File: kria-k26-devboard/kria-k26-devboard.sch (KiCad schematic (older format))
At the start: 2 parts

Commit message: Added second ETH interface, connect POE PSE
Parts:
- removed N?: antmicro_logo, antmicro-footprints:antmicro-logo, symbol antmicroMechanicalParts:antmicro_logo
- gave numbers to parts that had none: 1
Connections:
- wire segments 283 -> 289
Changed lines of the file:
@@
 F1 "eth.sch" 50
 F2 "MIO[64..77]" I L 9850 1200 50
-F3 "POE_VC[1..4]" I L 9850 900 50
+F3 "POE_VC[1..4]" I L 9850 850 50
 F4 "ETH_RESET" I R 11550 900 50
-$EndSheet
-$Sheet
-S 4350 800  1600 900
+F5 "VDD_POE_OUT" I L 9850 950 50
+F6 "VSS_POE_OUT" I L 9850 1050 50
+$EndSheet
+$Sheet
+S 4350 650  1600 1100
 U 63C44BC2
 F0 "Power Supply" 50
 F1 "supply.sch" 50
 F2 "PD_CC[1..2]" I R 5950 1550 50
-F3 "VCCOEN_PS_M2C" I R 5950 1000 50
-F4 "VCCOEN_PL_M2C" I R 5950 1100 50
-F5 "POE_VC[1..4]" I R 5950 900 50
-F6 "DBG_USB_P" I R 5950 1250 50
-F7 "DBG_USB_N" I R 5950 1400 50
+F3 "VCCOEN_PS_M2C" I R 5950 1100 50
+F4 "VCCOEN_PL_M2C" I R 5950 1200 50
+F5 "POE_VC[1..4]" I R 5950 700 50
+F6 "DBG_USB_P" I R 5950 1300 50
+F7 "DBG_USB_N" I R 5950 1450 50
 F8 "VBUS" I R 5950 1650 50
+F9 "VDD_POE_OUT" I R 5950 850 50
+F10 "VSS_POE_OUT" I R 5950 950 50
 $EndSheet
 $Sheet
@@
 F13 "~PS_POR" I L 4350 3150 50
 $EndSheet
-Wire Bus Line
-	5950 900  9850 900
-Wire Wire Line
-	5950 1100 6400 1100
+Wire Wire Line
+	5950 1200 6400 1200
 $Sheet
 S 9850 5250 1700 1300
@@
 	6000 2250 6000 2300
 Wire Wire Line
-	6250 1350 6000 1350
-Wire Wire Line
-	6000 1350 6000 1400
-Wire Wire Line
-	6000 1400 5950 1400
-Wire Wire Line
 	6000 2300 6250 2300
 Wire Wire Line
-	5950 1000 6500 1000
-Wire Wire Line
 	6500 1200 7050 1200
 Wire Wire Line
 	6400 1300 7050 1300
-Wire Wire Line
-	5950 1250 6000 1250
-Wire Wire Line
-	6000 1250 6000 1300
-Wire Wire Line
-	6000 1300 6300 1300
 Wire Wire Line
 	6300 2350 6000 2350
@@
 Wire Wire Line
 	7000 6300 6000 6300
-Wire Wire Line
-	6500 1000 6500 1200
-Wire Wire Line
-	6400 1100 6400 1300
 Wire Bus Line
 	6150 1550 5950 1550
 Wire Wire Line
-	6250 1350 6250 2300
-Wire Wire Line
-	6300 1300 6300 2350
-Wire Wire Line
 	5950 2000 6050 2000
 Wire Wire Line
 	6050 2000 6050 1650
-Wire Wire Line
-	6050 1650 5950 1650
 Wire Bus Line
 	5950 2100 6150 2100
@@
 	11650 8400 11650 10150
 $Comp
-L antmicroMechanicalParts:oshw_logo N?
+L antmicroMechanicalParts:oshw_logo N2
 U 1 1 63FCC534
 P 700 11000
-F 0 "N?" H 894 11003 50  0000 L CNN
+F 0 "N2" H 894 11003 50  0000 L CNN
 F 1 "oshw_logo" H 894 10912 50  0000 L CNN
 F 2 "antmicro-footprints:oshw-logo" H 720 10760 50  0001 C CNN
@@
 	1    0    0    -1
 $EndComp
-$Comp
-L antmicroMechanicalParts:antmicro_logo N?
-U 1 1 63FCC88F
-P 650 10850
-F 0 "N?" H 864 10943 50  0000 L CNN
-F 1 "antmicro_logo" H 864 10852 50  0000 L CNN
-F 2 "antmicro-footprints:antmicro-logo" H 550 11100 50  0001 C CNN
-F 3 "" H 650 11200 50  0001 C CNN
-	1    650  10850
-	1    0    0    -1
-$EndComp
 $Sheet
 S 9850 8700 1700 650
@@
 Wire Wire Line
 	6350 8250 7050 8250
+Wire Wire Line
+	6000 1300 6000 1350
+Wire Wire Line
+	5950 1300 6000 1300
+Wire Wire Line
+	6000 1450 5950 1450
+Wire Wire Line
+	6000 1400 6000 1450
+Wire Wire Line
+	6250 1400 6000 1400
+Wire Wire Line
+	6250 1400 6250 2300
+Wire Wire Line
+	6300 1350 6300 2350
+Wire Wire Line
+	6000 1350 6300 1350
+Wire Wire Line
+	6400 1200 6400 1300
+Wire Wire Line
+	6500 1100 6500 1200
+Wire Wire Line
+	5950 1100 6500 1100
+Wire Wire Line
+	6050 1650 5950 1650
+Wire Bus Line
+	5950 700  9700 700
+Wire Bus Line
+	9700 700  9700 850
+Wire Bus Line
+	9700 850  9850 850
+Wire Wire Line
+	9850 950  9600 950
+Wire Wire Line
+	9600 950  9600 850
+Wire Wire Line
+	9600 850  5950 850
+Wire Wire Line
+	9850 1050 9500 1050
+Wire Wire Line
+	9500 1050 9500 950
+Wire Wire Line
+	9500 950  5950 950
 $EndSCHEMATC

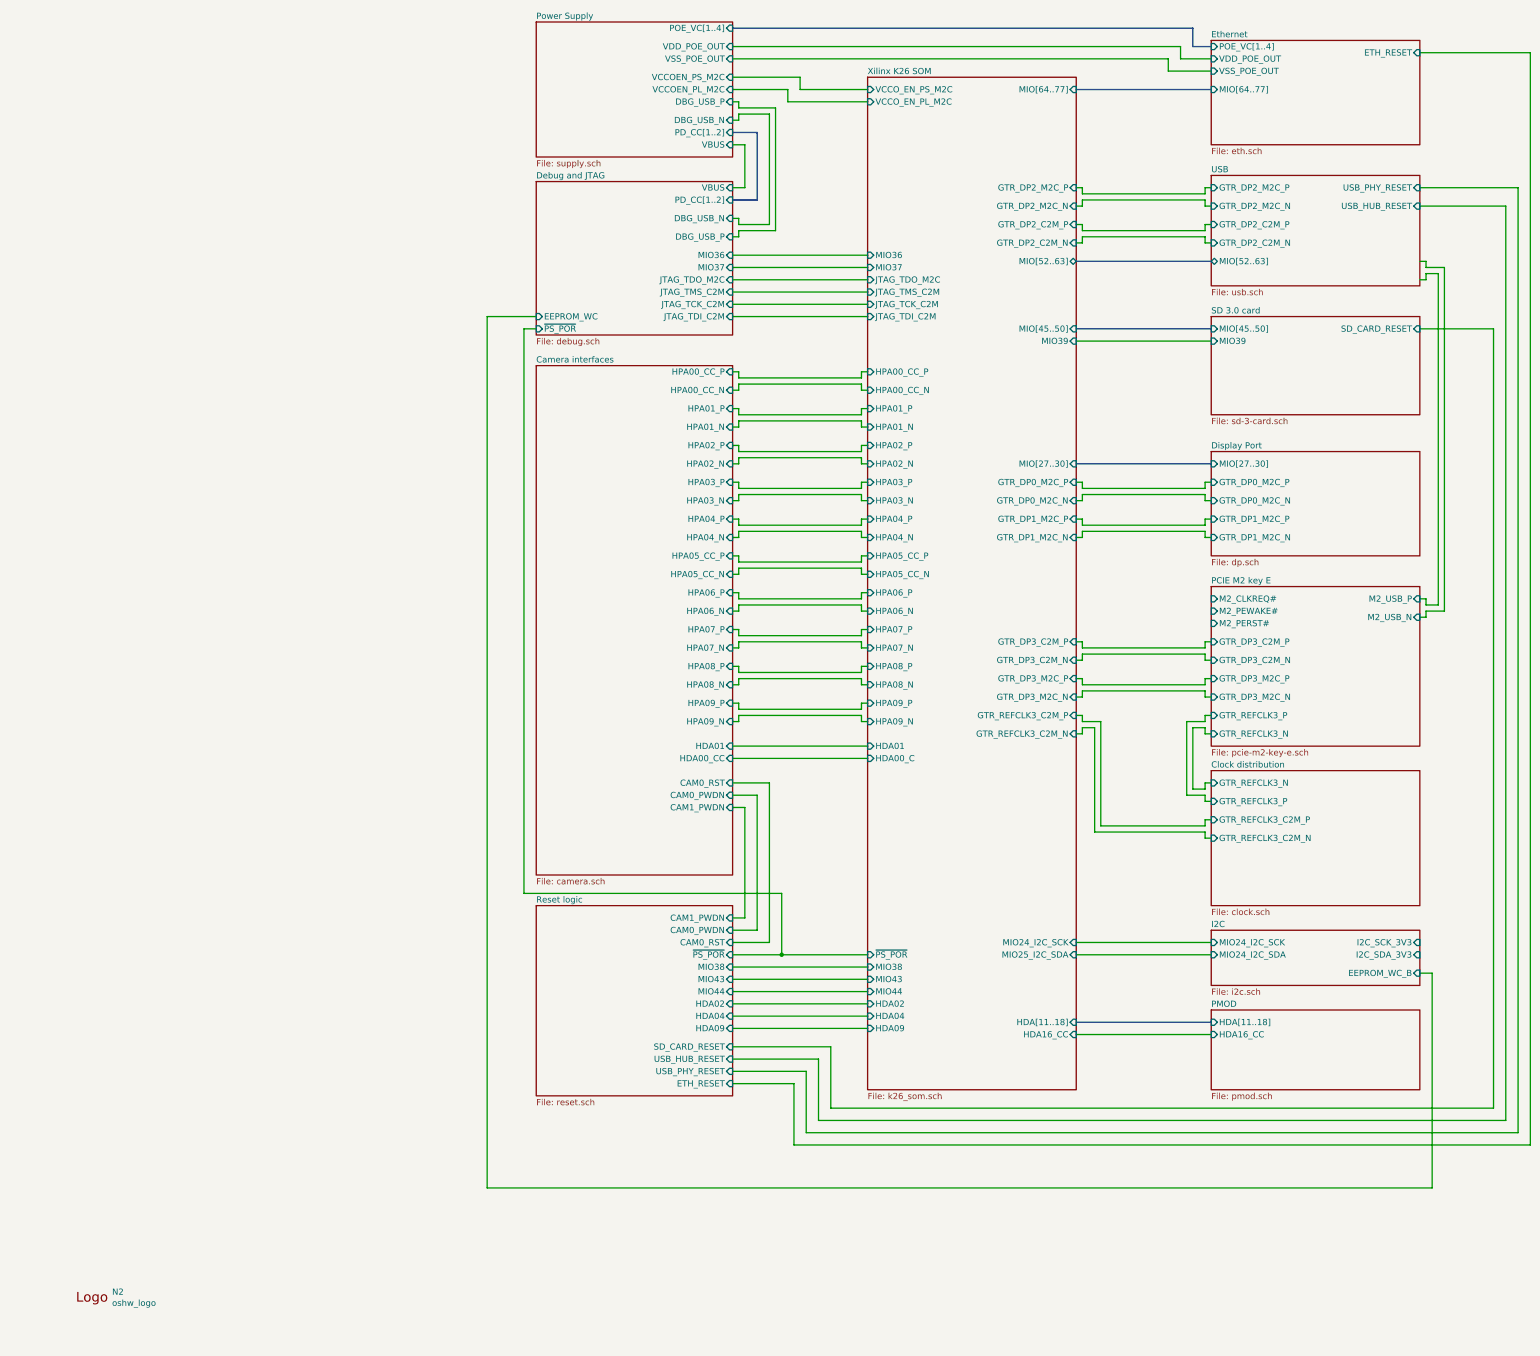
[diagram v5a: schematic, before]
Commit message: Fixes on Reset pagae, progress through clock sheet
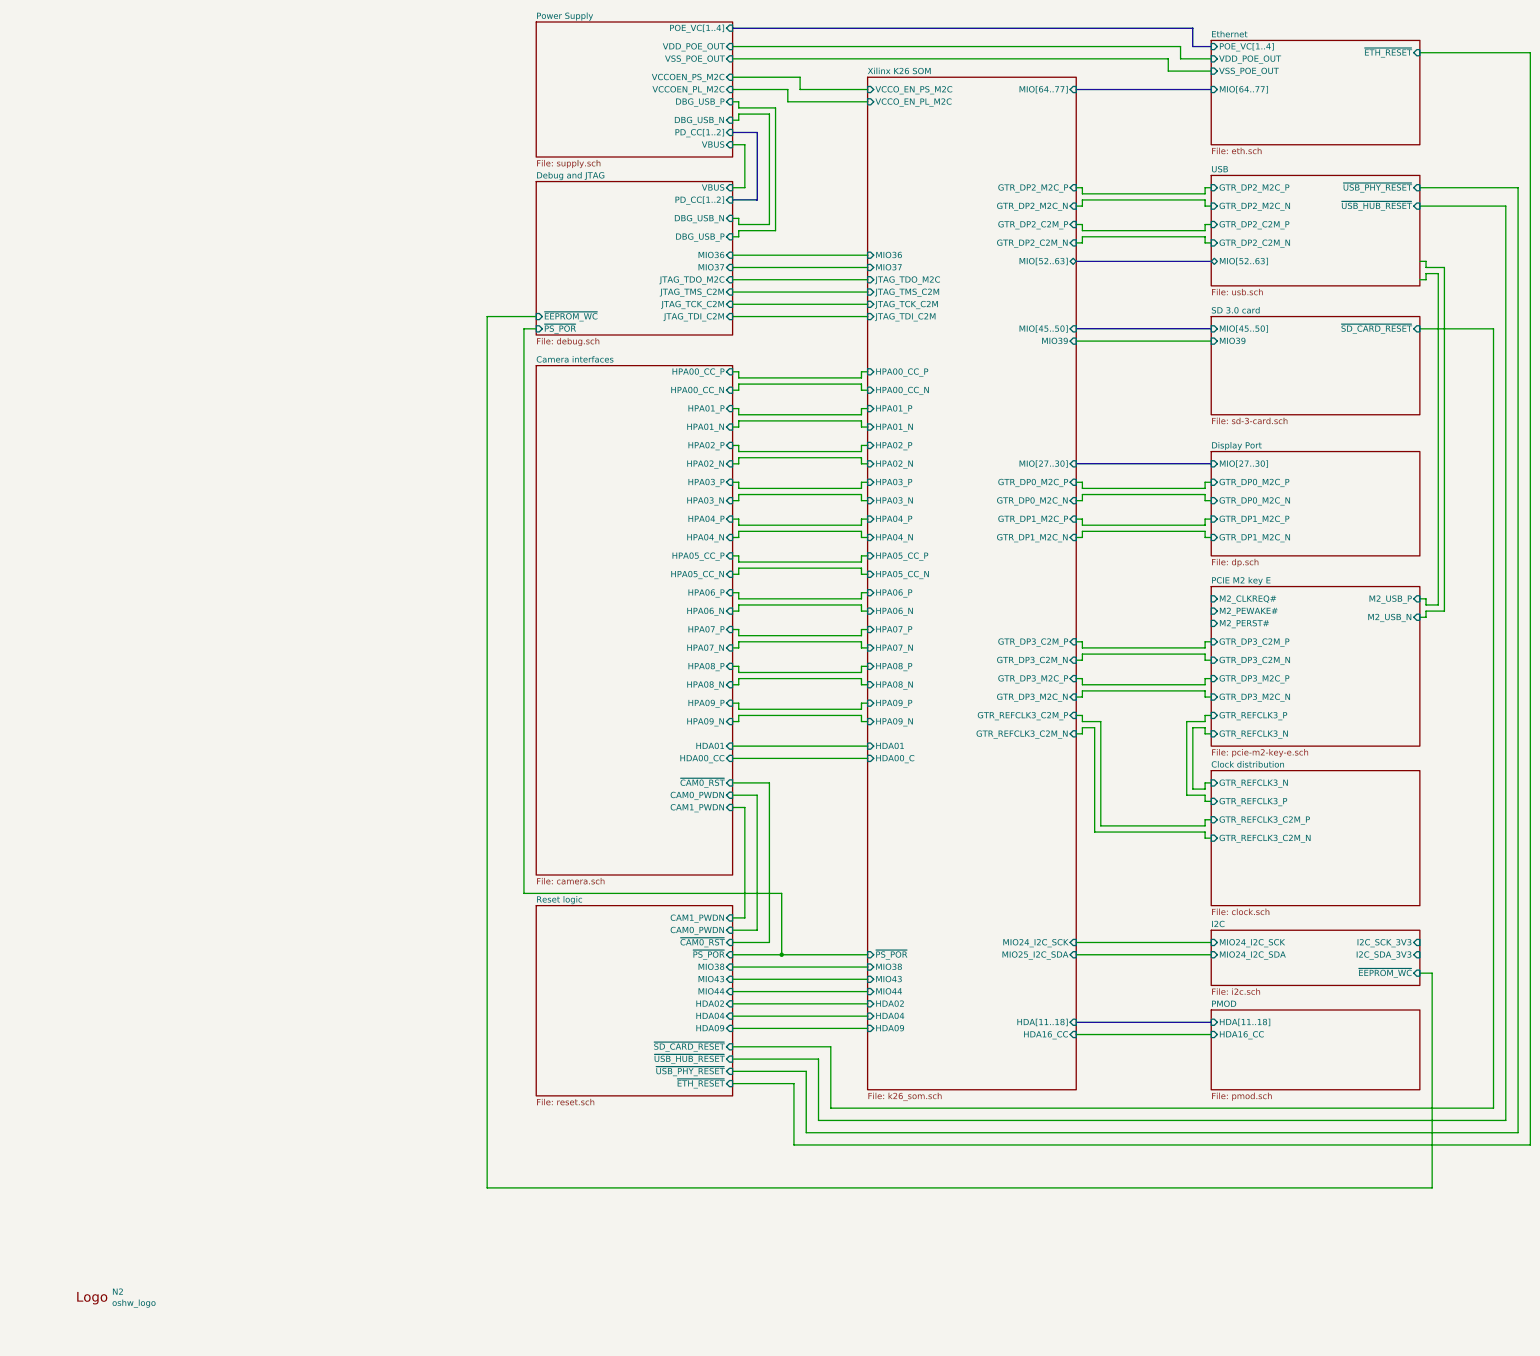
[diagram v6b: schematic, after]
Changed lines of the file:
@@
 $EndDescr
-$Sheet
-S 9850 800  1700 850
-U 63C3FA95
-F0 "Ethernet" 50
-F1 "eth.sch" 50
-F2 "MIO[64..77]" I L 9850 1200 50
-F3 "POE_VC[1..4]" I L 9850 850 50
-F4 "ETH_RESET" I R 11550 900 50
-F5 "VDD_POE_OUT" I L 9850 950 50
-F6 "VSS_POE_OUT" I L 9850 1050 50
-$EndSheet
 $Sheet
 S 4350 650  1600 1100
@@
 F9 "VDD_POE_OUT" I R 5950 850 50
 F10 "VSS_POE_OUT" I R 5950 950 50
-$EndSheet
-$Sheet
-S 9850 1900 1700 900
-U 63CADD16
-F0 "USB" 50
-F1 "usb.sch" 50
-F2 "MIO[52..63]" B L 9850 2600 50
-F3 "GTR_DP2_C2M_P" I L 9850 2300 50
-F4 "GTR_DP2_C2M_N" I L 9850 2450 50
-F5 "GTR_DP2_M2C_P" I L 9850 2000 50
-F6 "GTR_DP2_M2C_N" I L 9850 2150 50
-F7 "USB_PHY_RESET" I R 11550 2000 50
-F8 "USB_HUB_RESET" I R 11550 2150 50
 $EndSheet
 $Sheet
@@
 F10 "MIO36" I R 5950 2550 50
 F11 "VBUS" I R 5950 2000 50
-F12 "EEPROM_WC" I L 4350 3050 50
-F13 "~PS_POR" I L 4350 3150 50
+F12 "~PS_POR" I L 4350 3150 50
+F13 "~EEPROM_WC" I L 4350 3050 50
 $EndSheet
 Wire Wire Line
@@
 F2 "MIO[45..50]" I L 9850 3150 50
 F3 "MIO39" I L 9850 3250 50
-F4 "SD_CARD_RESET" I R 11550 3150 50
+F4 "~SD_CARD_RESET" I R 11550 3150 50
 $EndSheet
 Wire Wire Line
@@
 F22 "HDA01" I R 5950 6550 50
 F23 "HDA00_CC" I R 5950 6650 50
-F24 "CAM0_RST" I R 5950 6850 50
-F25 "CAM0_PWDN" I R 5950 6950 50
-F26 "CAM1_PWDN" I R 5950 7050 50
+F24 "CAM0_PWDN" I R 5950 6950 50
+F25 "CAM1_PWDN" I R 5950 7050 50
+F26 "~CAM0_RST" I R 5950 6850 50
 $EndSheet
 Wire Wire Line
@@
 F0 "Reset logic" 50
 F1 "reset.sch" 50
-F2 "SD_CARD_RESET" I R 5950 9000 50
-F3 "USB_PHY_RESET" I R 5950 9200 50
-F4 "USB_HUB_RESET" I R 5950 9100 50
-F5 "ETH_RESET" I R 5950 9300 50
-F6 "MIO43" I R 5950 8450 50
-F7 "MIO44" I R 5950 8550 50
-F8 "MIO38" I R 5950 8350 50
-F9 "CAM0_RST" I R 5950 8150 50
-F10 "CAM0_PWDN" I R 5950 8050 50
-F11 "CAM1_PWDN" I R 5950 7950 50
-F12 "HDA02" I R 5950 8650 50
-F13 "HDA04" I R 5950 8750 50
-F14 "HDA09" I R 5950 8850 50
-F15 "~PS_POR" I R 5950 8250 50
+F2 "MIO43" I R 5950 8450 50
+F3 "MIO44" I R 5950 8550 50
+F4 "MIO38" I R 5950 8350 50
+F5 "CAM0_PWDN" I R 5950 8050 50
+F6 "CAM1_PWDN" I R 5950 7950 50
+F7 "HDA02" I R 5950 8650 50
+F8 "HDA04" I R 5950 8750 50
+F9 "HDA09" I R 5950 8850 50
+F10 "~PS_POR" I R 5950 8250 50
+F11 "~USB_PHY_RESET" I R 5950 9200 50
+F12 "~USB_HUB_RESET" I R 5950 9100 50
+F13 "~ETH_RESET" I R 5950 9300 50
+F14 "~CAM0_RST" I R 5950 8150 50
+F15 "~SD_CARD_RESET" I R 5950 9000 50
 $EndSheet
 Wire Wire Line
@@
 F4 "I2C_SDA_3V3" I R 11550 8250 50
 F5 "I2C_SCK_3V3" I R 11550 8150 50
-F6 "EEPROM_WC_B" I R 11550 8400 50
+F6 "~EEPROM_WC" I R 11550 8400 50
 $EndSheet
 Wire Wire Line
@@
 Wire Wire Line
 	9500 950  5950 950
+$Sheet
+S 9850 1900 1700 900
+U 63CADD16
+F0 "USB" 50
+F1 "usb.sch" 50
+F2 "MIO[52..63]" B L 9850 2600 50
+F3 "GTR_DP2_C2M_P" I L 9850 2300 50
+F4 "GTR_DP2_C2M_N" I L 9850 2450 50
+F5 "GTR_DP2_M2C_P" I L 9850 2000 50
+F6 "GTR_DP2_M2C_N" I L 9850 2150 50
+F7 "~USB_PHY_RESET" I R 11550 2000 50
+F8 "~USB_HUB_RESET" I R 11550 2150 50
+$EndSheet
+$Sheet
+S 9850 800  1700 850
+U 63C3FA95
+F0 "Ethernet" 50
+F1 "eth.sch" 50
+F2 "MIO[64..77]" I L 9850 1200 50
+F3 "POE_VC[1..4]" I L 9850 850 50
+F4 "VDD_POE_OUT" I L 9850 950 50
+F5 "VSS_POE_OUT" I L 9850 1050 50
+F6 "~ETH_RESET" I R 11550 900 50
+$EndSheet
 $EndSCHEMATC

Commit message: Finished clock sheet
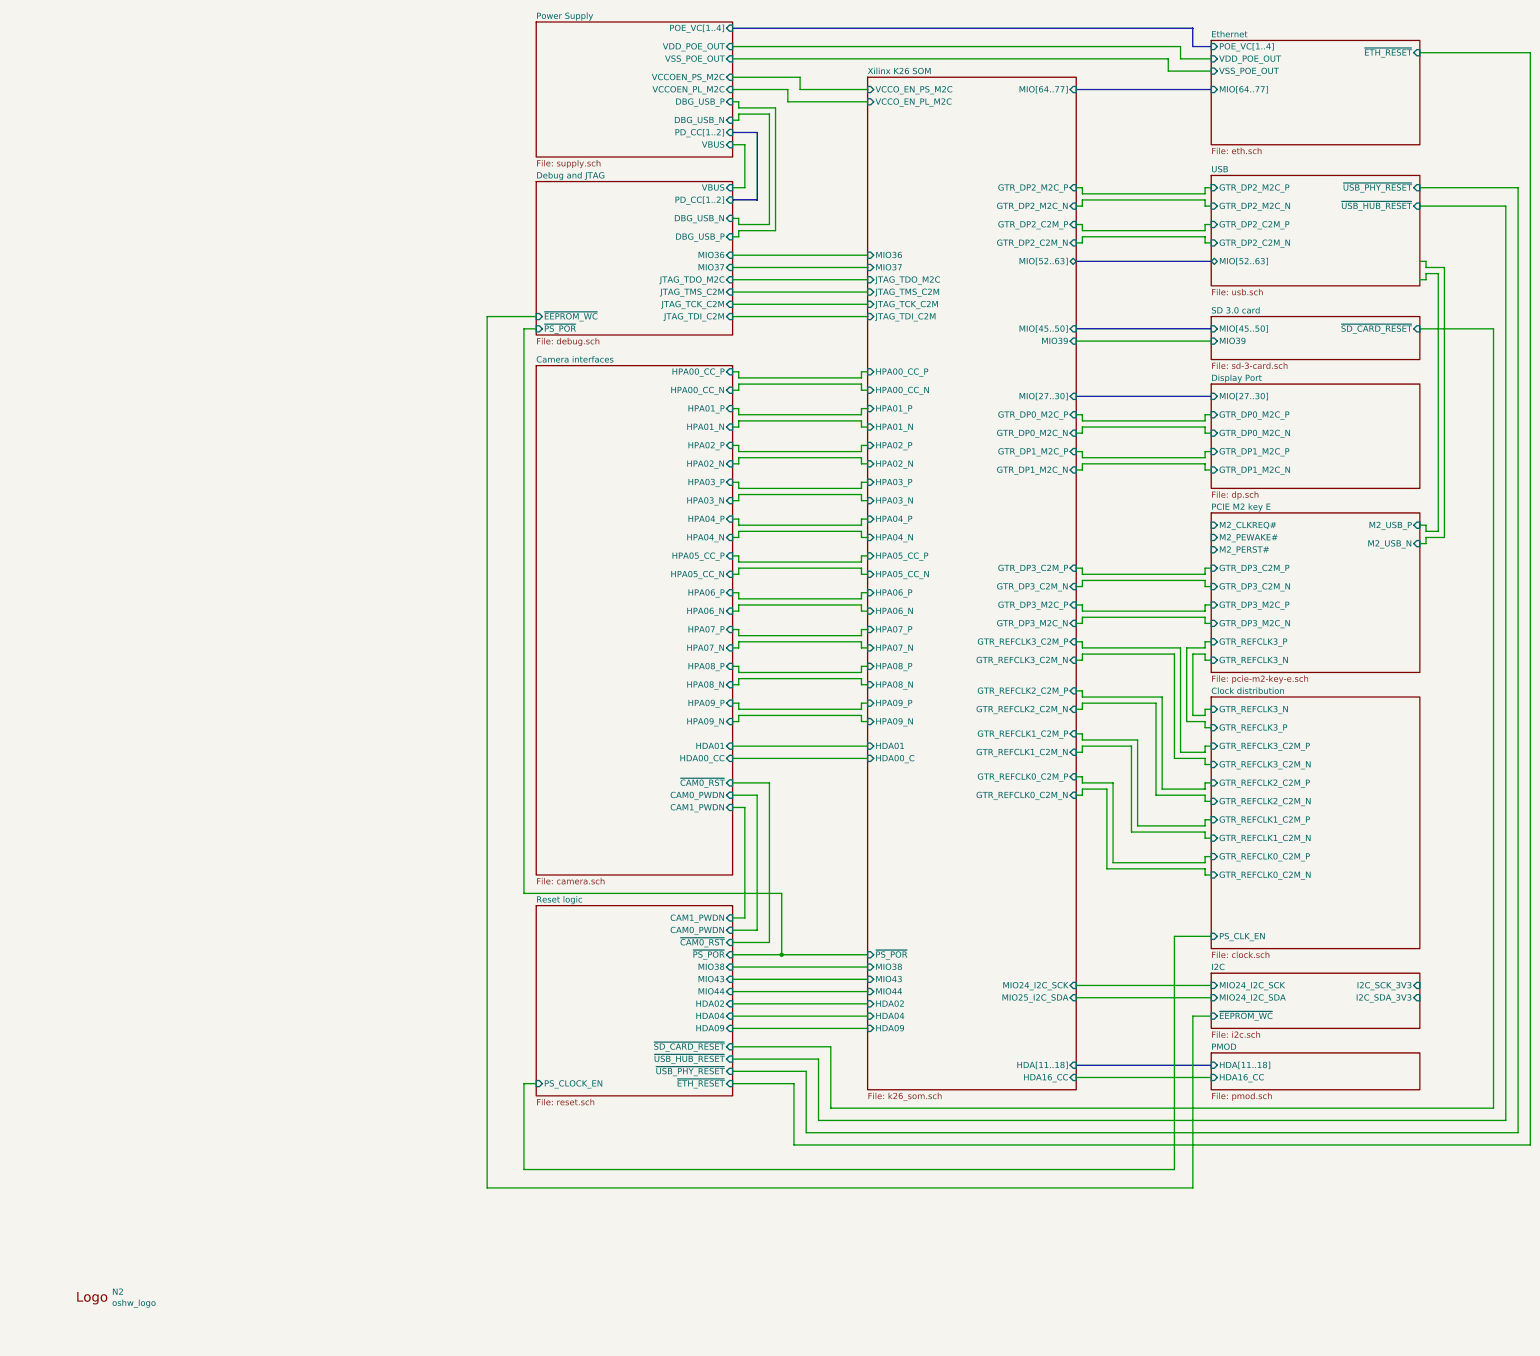
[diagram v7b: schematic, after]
